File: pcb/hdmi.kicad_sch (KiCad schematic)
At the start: 11 parts, among them J14 HDMI-A_HDMI-19PIN-043, U17 AP22615AWU-7

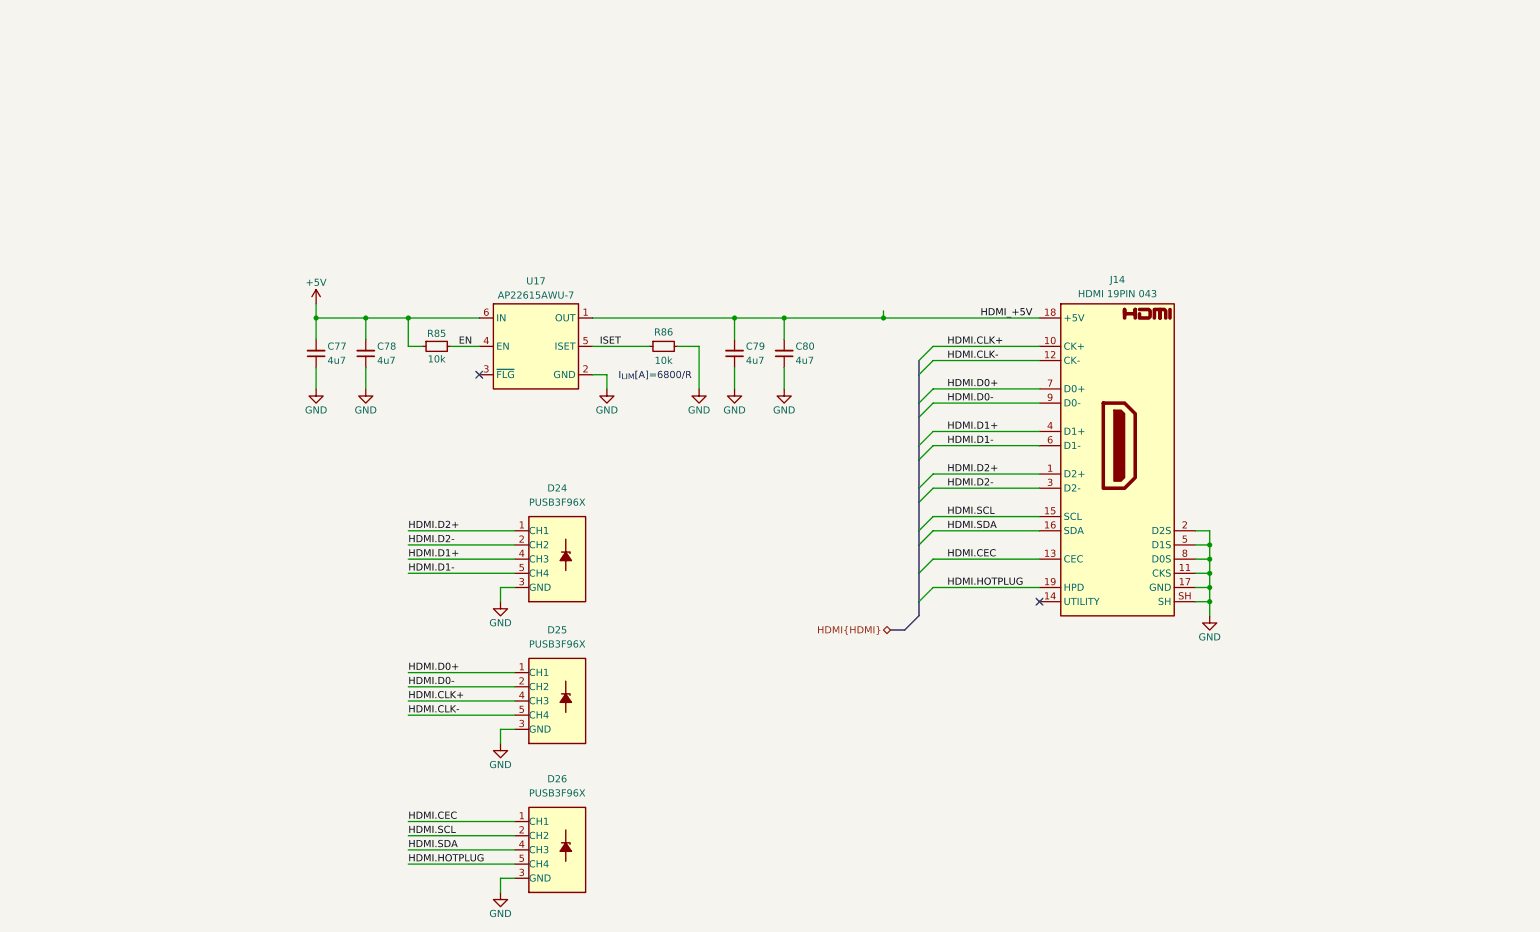
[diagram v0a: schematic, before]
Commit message: [#5] Refactor the schematic
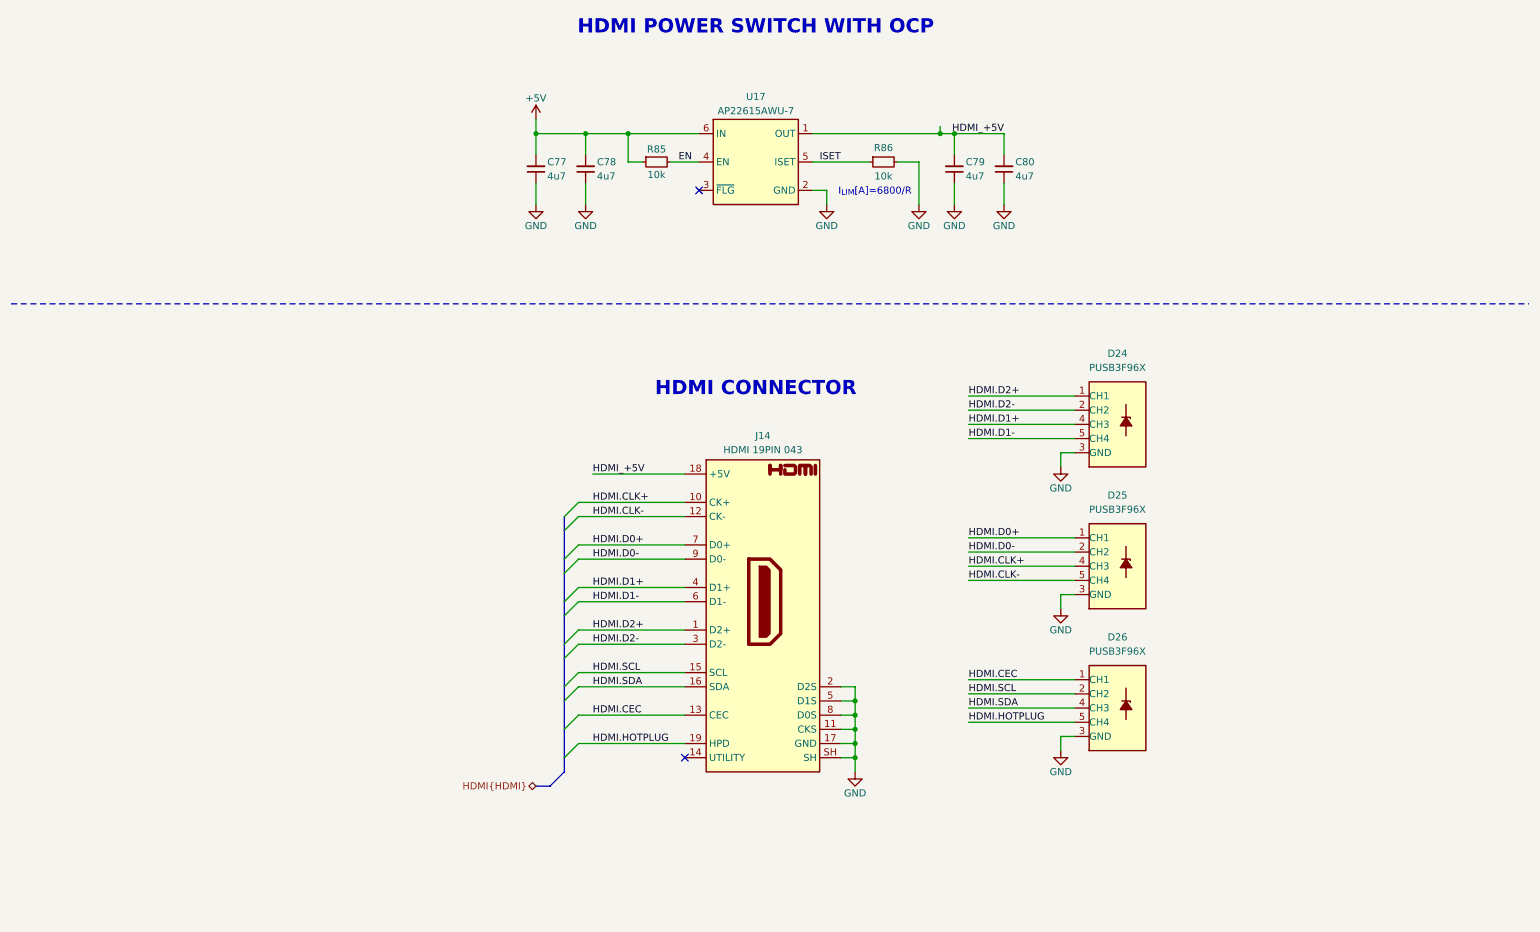
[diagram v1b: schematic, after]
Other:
- note added: "HDMI CONNECTOR"
- note added: "HDMI POWER SWITCH WITH OCP"
- moved on the sheet: C77, C78, C79, C80, D24, D25, D26, J14, R85, R86, U17
